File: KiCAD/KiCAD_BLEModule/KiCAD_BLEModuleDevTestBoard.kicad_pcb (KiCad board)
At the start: 2 copper layers, 51.5 x 106 mm, 61 parts, among them J1 PinHeader2.54mm_8, J2 PinHeader2.54mm_2x16, J3 USB-TYPE-C-31-M-17, SW1 SW_Tact_1105, SW10 SW_Tact_1105, SW11 SW_Tact_1105, SW12 SW_Tact_1105, SW13 SW_Tact_1105, SW14 SW_Tact_1105, SW15 SW_Tact_1105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

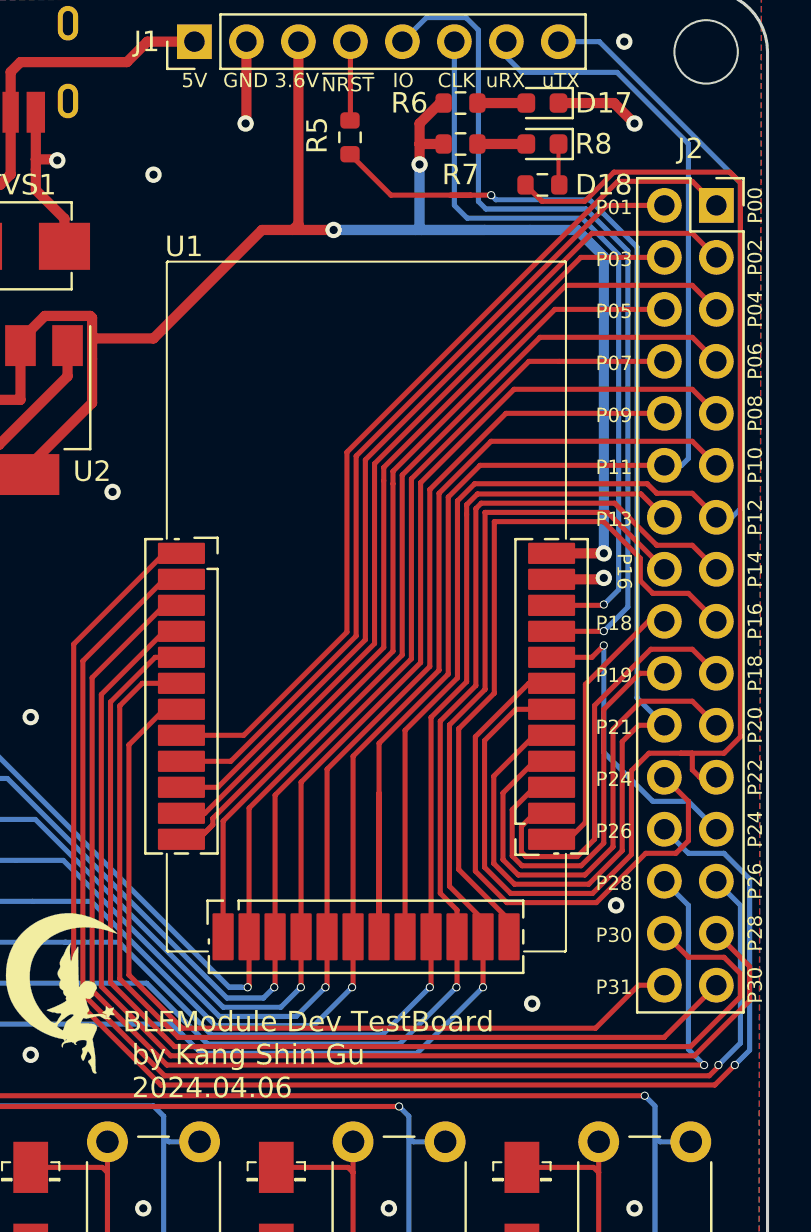
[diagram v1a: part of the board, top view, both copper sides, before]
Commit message: KSG : 아트워크 프린트 오기 수정
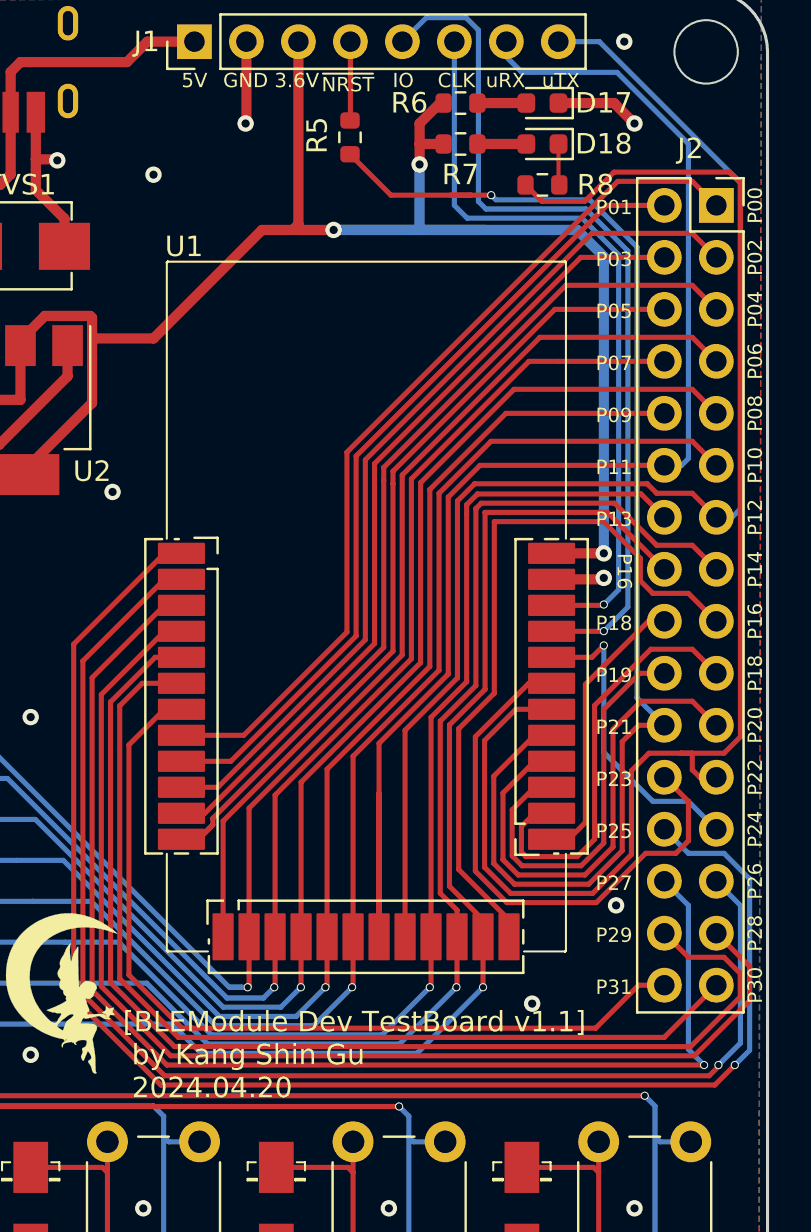
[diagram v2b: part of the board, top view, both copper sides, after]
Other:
- board text added: "P23"
- board text added: "P25"
- board text added: "P27"
- board text added: "P29"
- board text added: "[BLEModule Dev TestBoard v1.1] by Kang Shin Gu 2024.04.20"
- board text removed: "BLEModule Dev TestBoard by Kang Shin Gu 2024.04.06"
